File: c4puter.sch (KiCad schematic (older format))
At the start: 26 parts, among them J7 19V 3A, J9 PANEL, Q1 AOD4189, Q2 AOD4189, SW1 POWER, SW2 SW

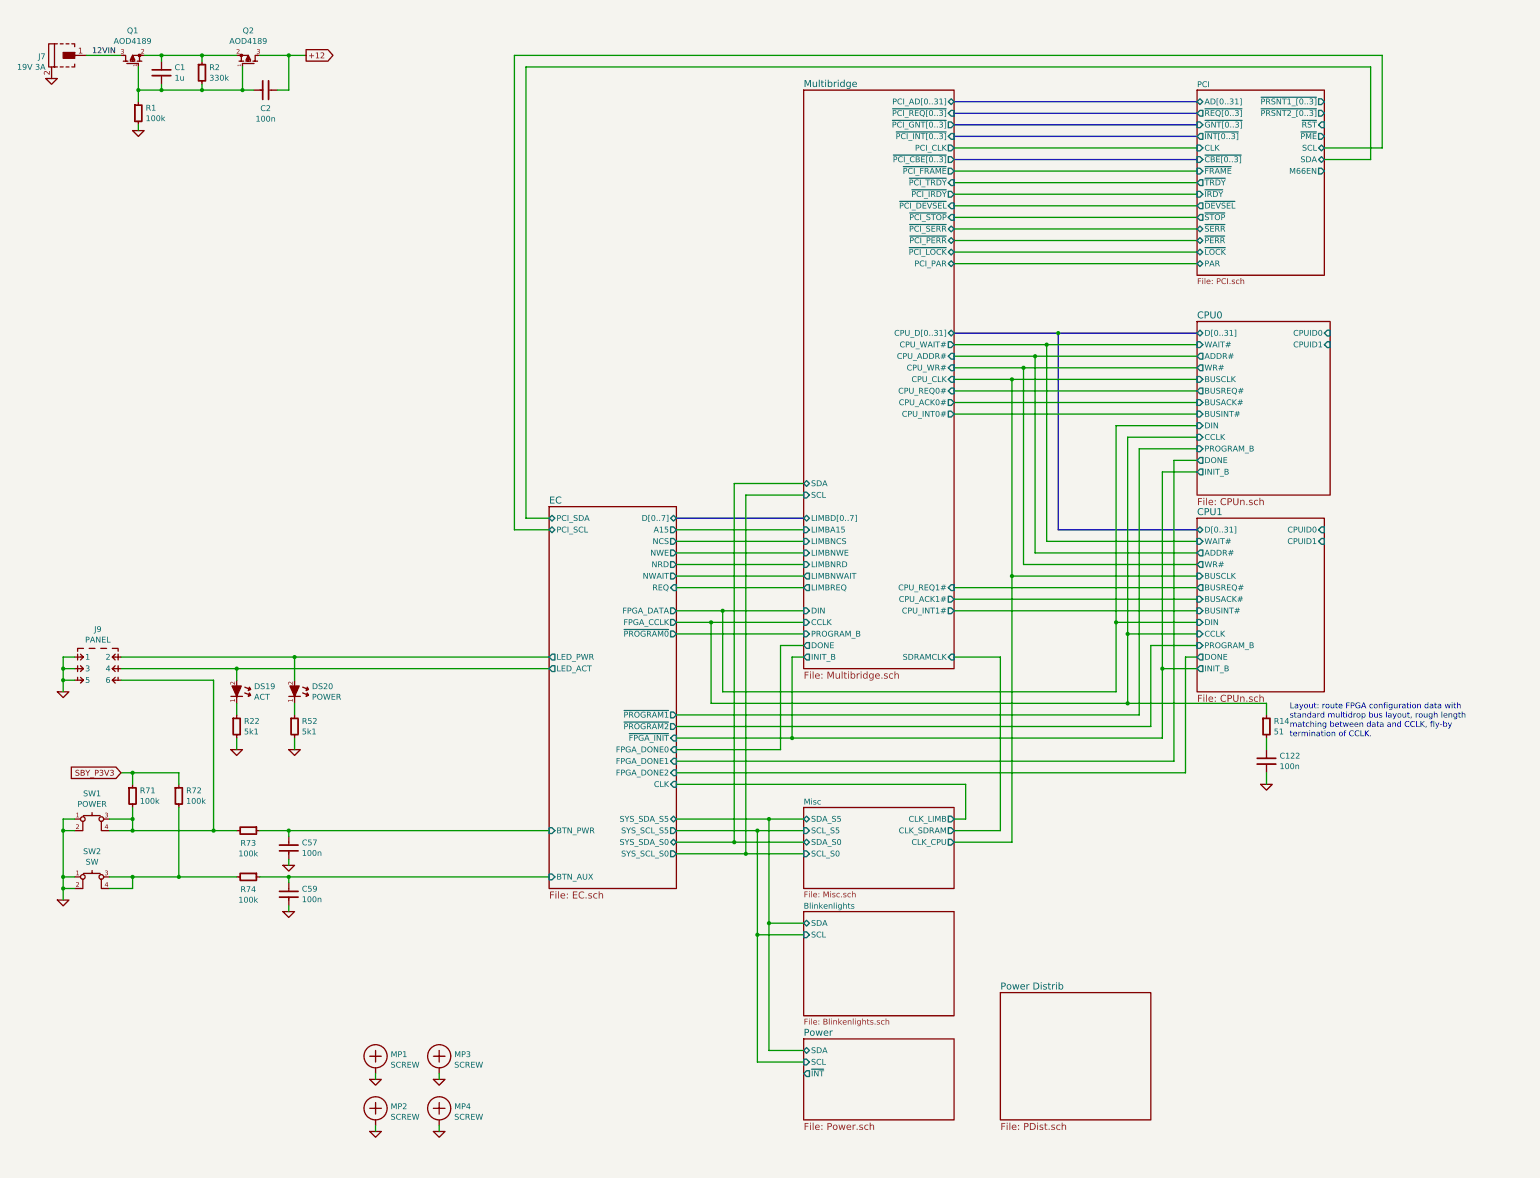
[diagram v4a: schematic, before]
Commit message: Route PCI utility lines
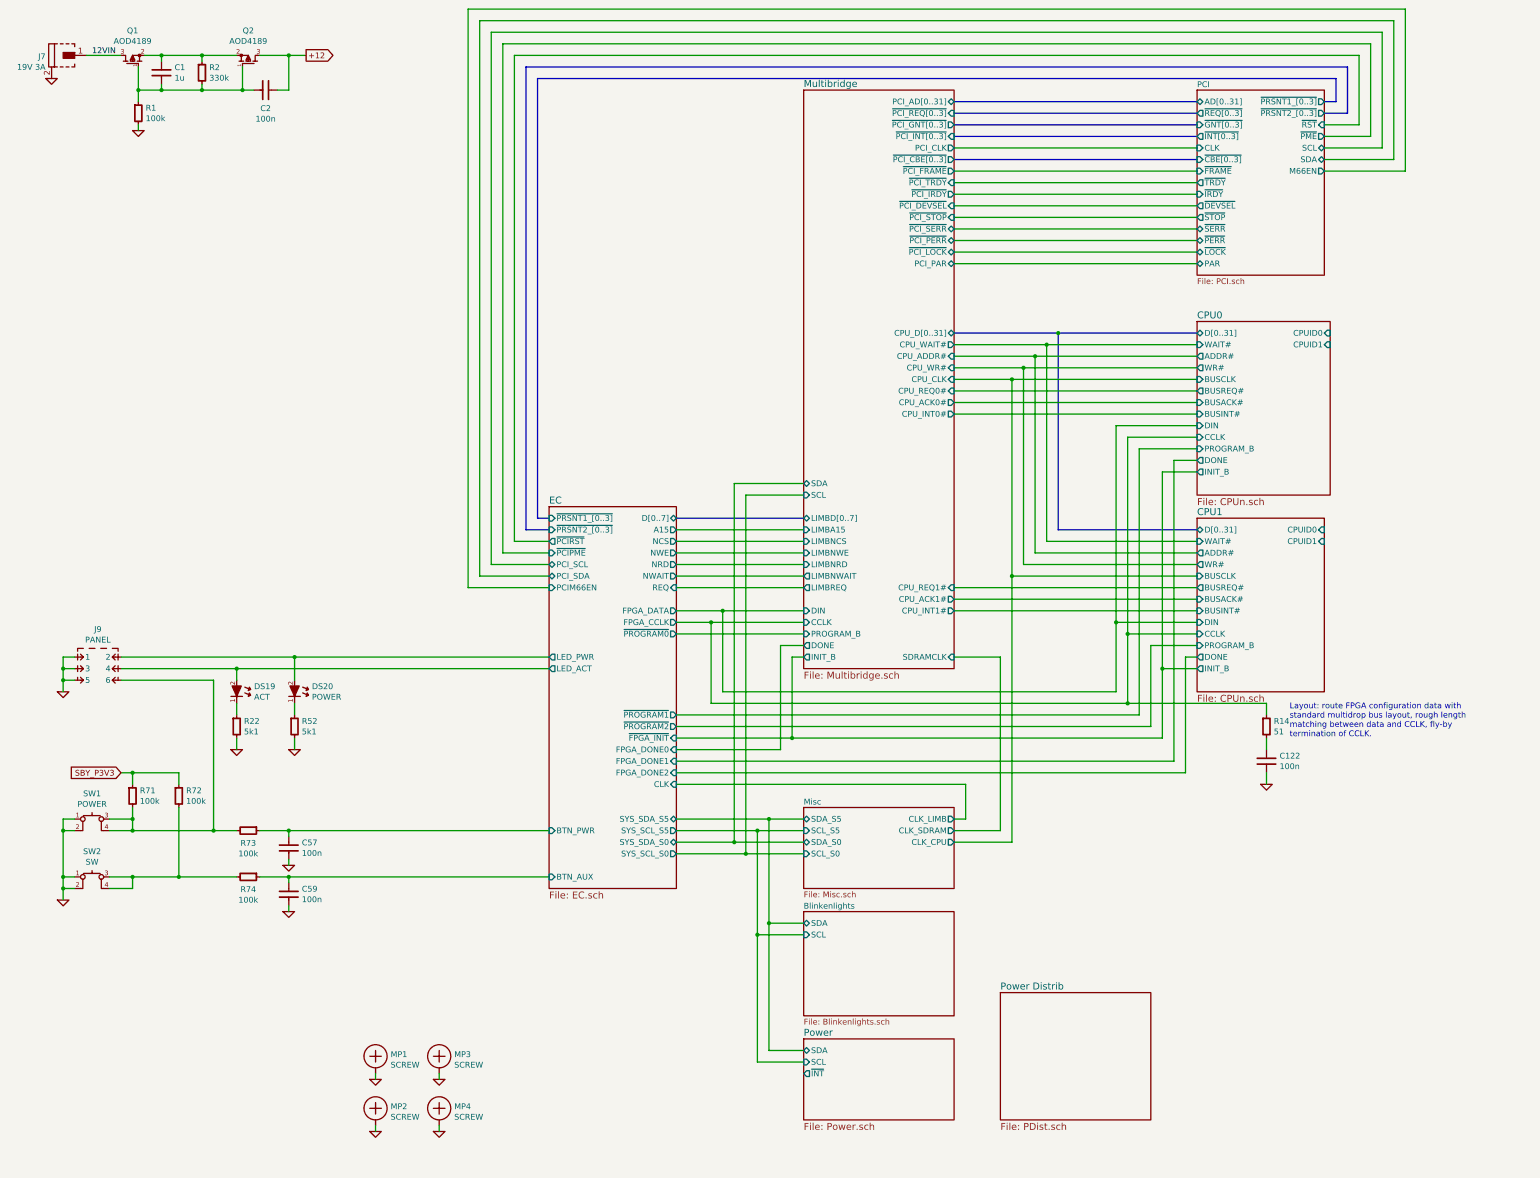
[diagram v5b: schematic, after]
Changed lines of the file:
@@
 	6700 5600 6700 6300
 Wire Wire Line
-	10100 6300 6700 6300
-Wire Wire Line
-	10100 4000 10100 6300
+	6700 6300 10100 6300
+Wire Wire Line
+	10100 6300 10100 4000
 Wire Wire Line
 	10100 4000 10800 4000
@@
 F25 "SYS_SDA_S0" B R 6300 7600 50
 F26 "CLK" I R 6300 7100 50
-F27 "PCI_SDA" B L 5200 4800 50
-F28 "PCI_SCL" B L 5200 4900 50
+F27 "PCI_SDA" B L 5200 5300 50
+F28 "PCI_SCL" B L 5200 5200 50
+F29 "~PRSNT1_[0..3]" I L 5200 4800 50
+F30 "~PRSNT2_[0..3]" I L 5200 4900 50
+F31 "~PCIRST" O L 5200 5000 50
+F32 "~PCIPME" I L 5200 5100 50
+F33 "PCIM66EN" I L 5200 5400 50
 $EndSheet
 Wire Wire Line
@@
 Connection ~ 6800 7600
 Wire Wire Line
-	5200 4800 5000 4800
-Wire Wire Line
-	5000 4800 5000 900
-Wire Wire Line
-	5000 900  12300 900
-Wire Wire Line
-	12300 900  12300 1700
-Wire Wire Line
-	12300 1700 11900 1700
-Wire Wire Line
-	5200 4900 4900 4900
-Wire Wire Line
-	4900 4900 4900 800
-Wire Wire Line
-	4900 800  12400 800
-Wire Wire Line
-	12400 800  12400 1600
+	5200 5300 4600 5300
+Wire Wire Line
+	4600 5300 4600 500
+Wire Wire Line
+	4600 500  12500 500
+Wire Wire Line
+	12500 500  12500 1700
+Wire Wire Line
+	12500 1700 11900 1700
+Wire Wire Line
+	5200 5200 4700 5200
+Wire Wire Line
+	4700 5200 4700 600
+Wire Wire Line
+	4700 600  12400 600
+Wire Wire Line
+	12400 600  12400 1600
 Wire Wire Line
 	12400 1600 11900 1600
+Wire Bus Line
+	5200 4800 5100 4800
+Wire Bus Line
+	5100 4800 5100 1000
+Wire Bus Line
+	5100 1000 12000 1000
+Wire Bus Line
+	12000 1000 12000 1200
+Wire Bus Line
+	12000 1200 11900 1200
+Wire Bus Line
+	5200 4900 5000 4900
+Wire Bus Line
+	5000 4900 5000 900
+Wire Bus Line
+	5000 900  12100 900
+Wire Bus Line
+	12100 900  12100 1300
+Wire Bus Line
+	12100 1300 11900 1300
+Wire Wire Line
+	5200 5100 4800 5100
+Wire Wire Line
+	4800 5100 4800 700
+Wire Wire Line
+	4800 700  12300 700
+Wire Wire Line
+	12300 700  12300 1500
+Wire Wire Line
+	12300 1500 11900 1500
+Wire Wire Line
+	5200 5000 4900 5000
+Wire Wire Line
+	4900 5000 4900 800
+Wire Wire Line
+	4900 800  12200 800
+Wire Wire Line
+	12200 800  12200 1400
+Wire Wire Line
+	12200 1400 11900 1400
+Wire Wire Line
+	5200 5400 4500 5400
+Wire Wire Line
+	4500 5400 4500 400
+Wire Wire Line
+	4500 400  12600 400
+Wire Wire Line
+	12600 400  12600 1800
+Wire Wire Line
+	12600 1800 11900 1800
 $EndSCHEMATC
